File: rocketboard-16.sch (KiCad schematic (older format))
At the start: 128 parts, among them J1 SWD, K1 MX_RGB, K10 MX_RGB, K11 MX_RGB, K12 MX_RGB, K13 MX_RGB, K14 MX_RGB, K15 MX_RGB, K16 MX_RGB, K2 MX_RGB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

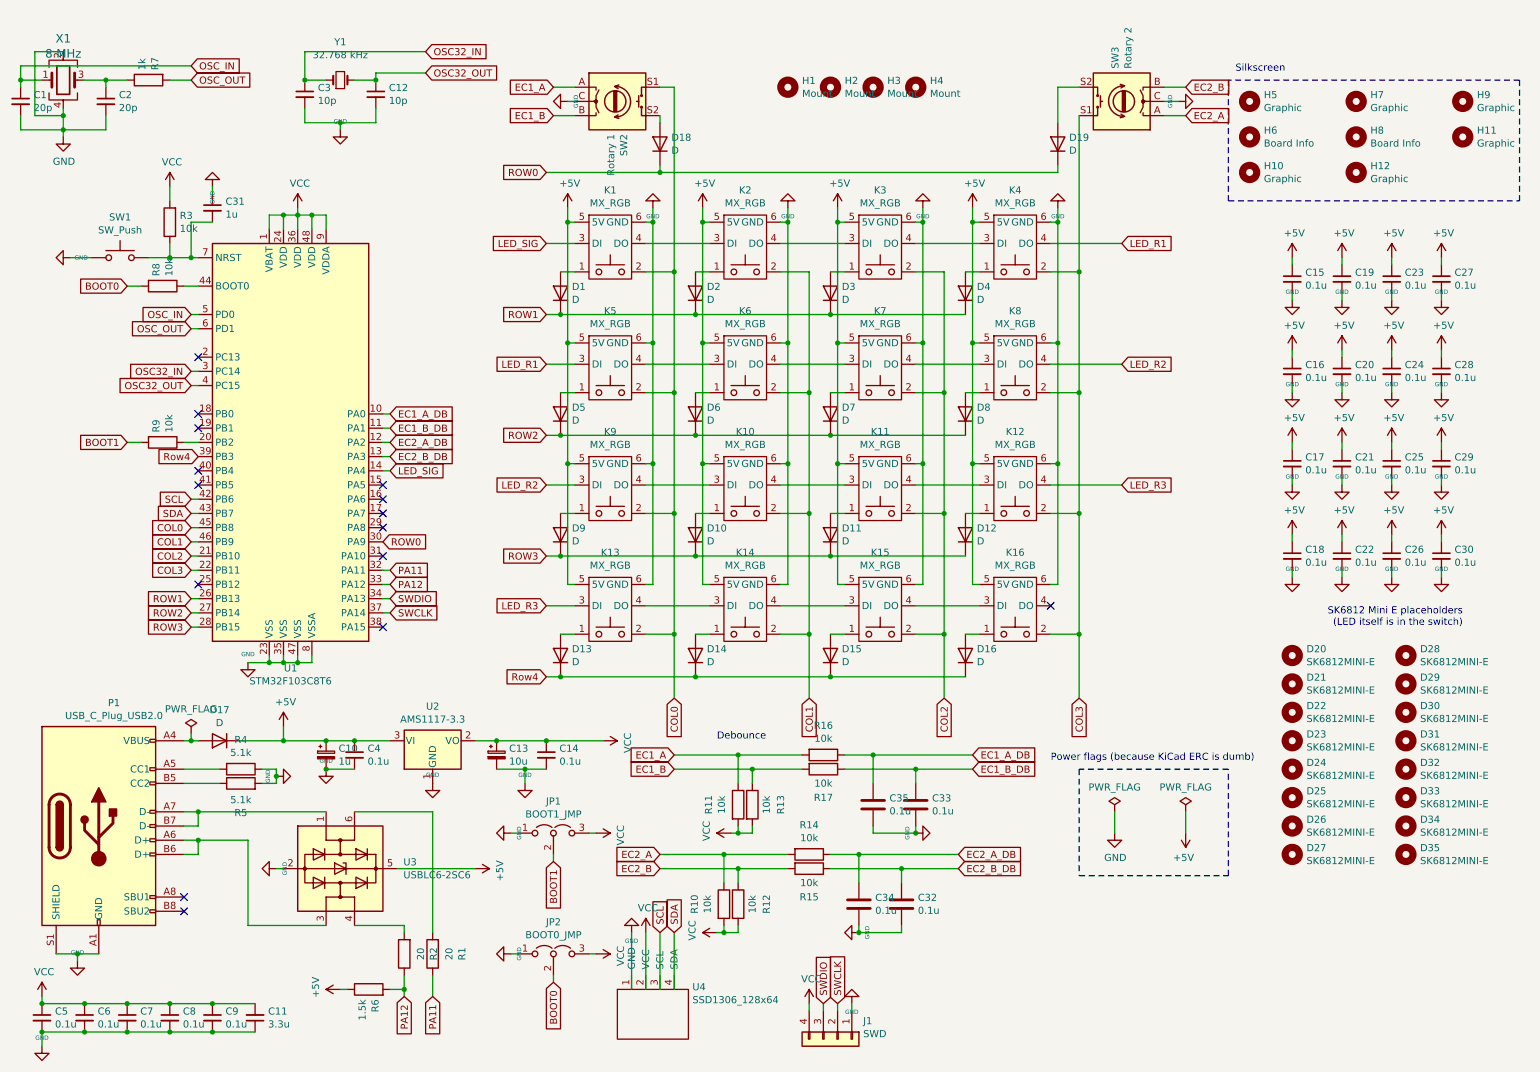
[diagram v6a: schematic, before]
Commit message: Added in a level shifting circuit for the LED signal (needs 5v sig, not 3.3v), added a 10uf cap on the 5v line for smoothing out possible spikey power draw from LEDs, and added test points on +5v, VCC, and GND
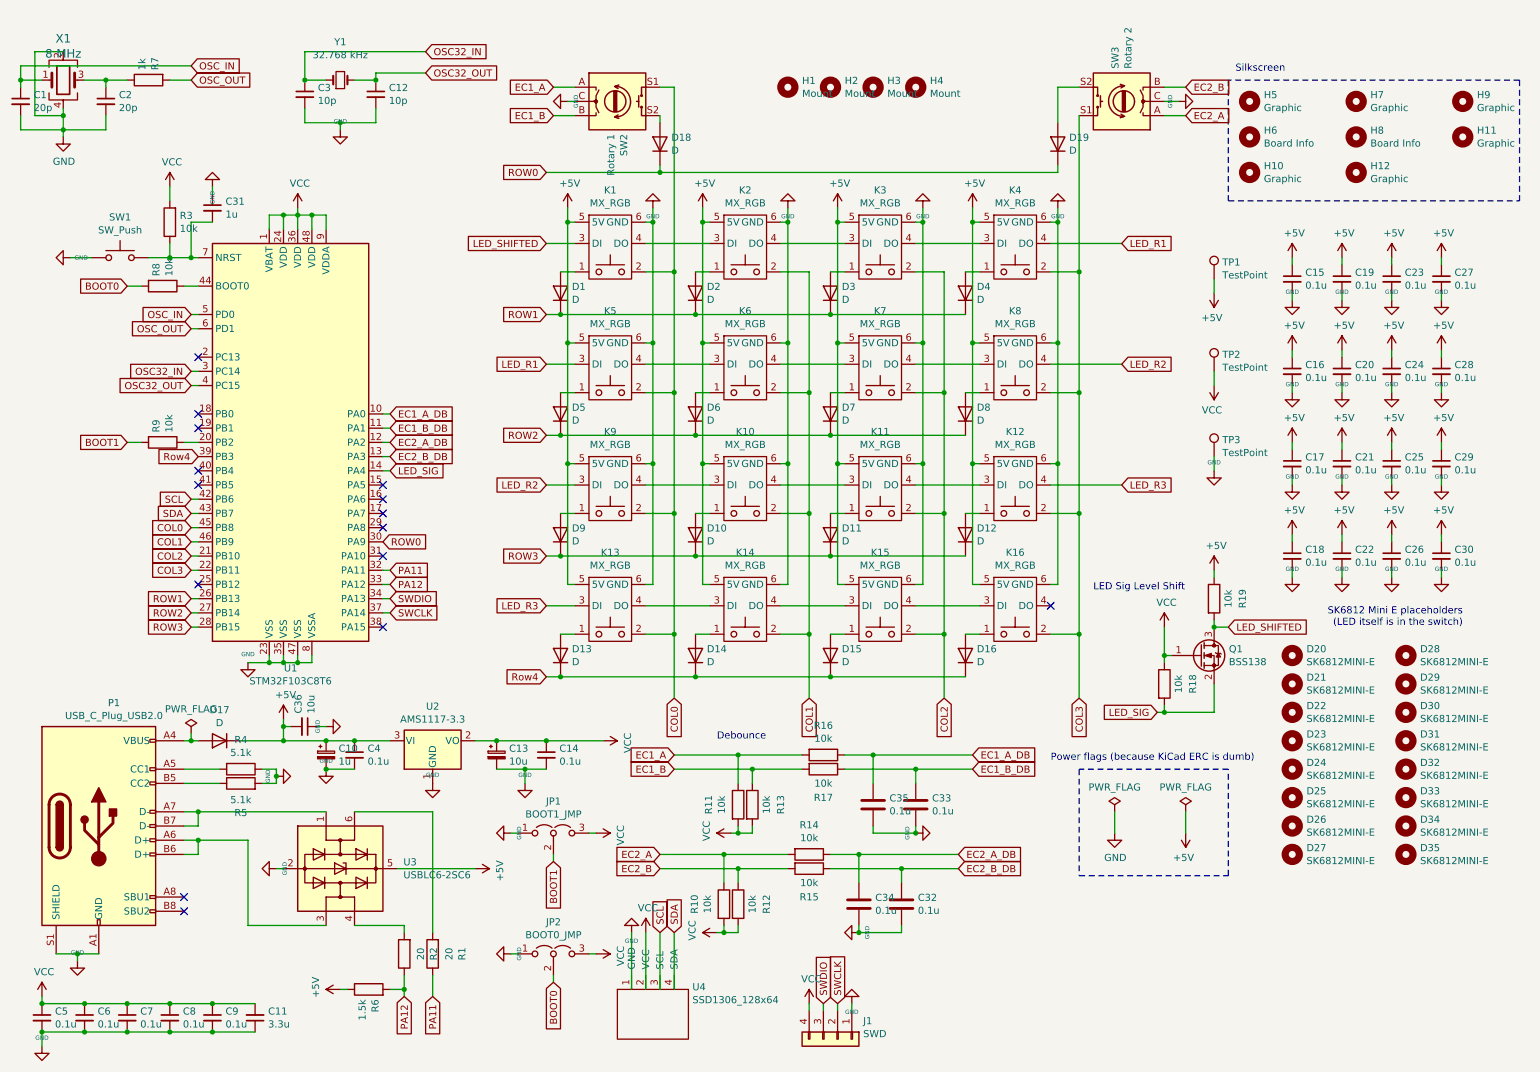
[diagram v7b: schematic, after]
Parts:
- added C36: 10u, Capacitor_SMD:C_0603_1608Metric, symbol Device:C_Small
- added Q1: BSS138, Package_TO_SOT_SMD:SOT-23, symbol Transistor_FET:BSS138
- added R18, R19: 10k, Resistor_SMD:R_0603_1608Metric, symbol Device:R
- added TP1, TP2, TP3: TestPoint, TestPoint:TestPoint_Pad_D1.0mm, symbol Connector:TestPoint
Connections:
- net +5V: now also C36.2, R19.1, TP1.1
- net GND: now also C36.1, TP3.1
- net LED_SIG: now also Q1.2 (S), R18.2; no longer K1.3 (DI)
- net VCC: now also Q1.1 (G), R18.1, TP2.1
- new net LED_SHIFTED: K1.3 (DI), Q1.3 (D), R19.2
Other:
- note added: "LED Sig Level Shift"
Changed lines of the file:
@@
 L power:+5V #PWR010
 U 1 1 5F3A3D06
-P 2450 5400
-F 0 "#PWR010" H 2450 5250 50  0001 C CNN
-F 1 "+5V" H 2465 5573 50  0000 C CNN
-F 2 "" H 2450 5400 50  0001 C CNN
-F 3 "" H 2450 5400 50  0001 C CNN
-	1    2450 5400
+P 2450 5350
+F 0 "#PWR010" H 2450 5200 50  0001 C CNN
+F 1 "+5V" H 2465 5523 50  0000 C CNN
+F 2 "" H 2450 5350 50  0001 C CNN
+F 3 "" H 2450 5350 50  0001 C CNN
+	1    2450 5350
 	1    0    0    -1
 $EndComp
@@
 Text GLabel 3200 3600 2    50   Input ~ 0
 LED_SIG
-Text GLabel 4300 2000 0    50   Input ~ 0
-LED_SIG
 $Comp
 L Device:R R7
@@
 Wire Wire Line
 	4300 5500 4700 5500
-Wire Wire Line
-	2450 5400 2450 5500
 Connection ~ 2450 5500
 Wire Wire Line
@@
 	1    0    0    -1
 $EndComp
+$Comp
+L Device:R R18
+U 1 1 5F971C6A
+P 8650 5100
+F 0 "R18" V 8850 5100 50  0000 C CNN
+F 1 "10k" V 8750 5100 50  0000 C CNN
+F 2 "Resistor_SMD:R_0603_1608Metric" V 8580 5100 50  0001 C CNN
+F 3 "~" H 8650 5100 50  0001 C CNN
+	1    8650 5100
+	1    0    0    -1
+$EndComp
+$Comp
+L Device:R R19
+U 1 1 5F9730D1
+P 9000 4500
+F 0 "R19" V 9200 4500 50  0000 C CNN
+F 1 "10k" V 9100 4500 50  0000 C CNN
+F 2 "Resistor_SMD:R_0603_1608Metric" V 8930 4500 50  0001 C CNN
+F 3 "~" H 9000 4500 50  0001 C CNN
+	1    9000 4500
+	1    0    0    -1
+$EndComp
+$Comp
+L Transistor_FET:BSS138 Q1
+U 1 1 5F9744B4
+P 8900 4900
+F 0 "Q1" H 9104 4946 50  0000 L CNN
+F 1 "BSS138" H 9104 4855 50  0000 L CNN
+F 2 "Package_TO_SOT_SMD:SOT-23" H 9100 4825 50  0001 L CIN
+F 3 "https://www.fairchildsemi.com/datasheets/BS/BSS138.pdf" H 8900 4900 50  0001 L CNN
+	1    8900 4900
+	1    0    0    -1
+$EndComp
+$Comp
+L power:+5V #PWR065
+U 1 1 5F97B5D2
+P 9000 4300
+F 0 "#PWR065" H 9000 4150 50  0001 C CNN
+F 1 "+5V" H 9015 4473 50  0000 C CNN
+F 2 "" H 9000 4300 50  0001 C CNN
+F 3 "" H 9000 4300 50  0001 C CNN
+	1    9000 4300
+	1    0    0    -1
+$EndComp
+$Comp
+L power:VCC #PWR064
+U 1 1 5F9A2AE6
+P 8650 4700
+F 0 "#PWR064" H 8650 4550 50  0001 C CNN
+F 1 "VCC" H 8665 4873 50  0000 C CNN
+F 2 "" H 8650 4700 50  0001 C CNN
+F 3 "" H 8650 4700 50  0001 C CNN
+	1    8650 4700
+	1    0    0    -1
+$EndComp
+Text GLabel 8600 5300 0    50   Input ~ 0
+LED_SIG
+Wire Wire Line
+	8650 4900 8700 4900
+Wire Wire Line
+	9000 4300 9000 4350
+Wire Wire Line
+	9000 4700 9000 4650
+Text GLabel 9100 4700 2    50   Input ~ 0
+LED_SHIFTED
+Wire Wire Line
+	9100 4700 9000 4700
+Connection ~ 9000 4700
+Text Notes 8150 4450 0    50   ~ 0
+LED Sig Level Shift
+Text GLabel 4300 2000 0    50   Input ~ 0
+LED_SHIFTED
+Wire Wire Line
+	8650 4700 8650 4900
+Wire Wire Line
+	8650 4950 8650 4900
+Connection ~ 8650 4900
+Wire Wire Line
+	8600 5300 8650 5300
+Wire Wire Line
+	9000 5300 9000 5100
+Wire Wire Line
+	8650 5250 8650 5300
+Connection ~ 8650 5300
+Wire Wire Line
+	8650 5300 9000 5300
+Wire Wire Line
+	2450 5350 2450 5400
+$Comp
+L Device:C_Small C36
+U 1 1 600E708F
+P 2600 5400
+F 0 "C36" H 2508 5354 50  0000 R CNN
+F 1 "10u" H 2508 5445 50  0000 R CNN
+F 2 "Capacitor_SMD:C_0603_1608Metric" H 2600 5400 50  0001 C CNN
+F 3 "~" H 2600 5400 50  0001 C CNN
+	1    2600 5400
+	0    1    1    0
+$EndComp
+Wire Wire Line
+	2450 5400 2500 5400
+Connection ~ 2450 5400
+Wire Wire Line
+	2450 5400 2450 5500
+$Comp
+L power:GND #PWR066
+U 1 1 60138915
+P 2750 5400
+F 0 "#PWR066" H 2750 5450 20  0001 C CNN
+F 1 "GND" H 2750 5459 30  0000 C CNN
+F 2 "" H 2750 5400 60  0000 C CNN
+F 3 "" H 2750 5400 60  0000 C CNN
+	1    2750 5400
+	0    -1   -1   0
+$EndComp
+Wire Wire Line
+	2700 5400 2750 5400
+$Comp
+L Connector:TestPoint TP1
+U 1 1 6018BF84
+P 9000 2250
+F 0 "TP1" H 9058 2368 50  0000 L CNN
+F 1 "TestPoint" H 9058 2277 50  0000 L CNN
+F 2 "TestPoint:TestPoint_Pad_D1.0mm" H 9200 2250 50  0001 C CNN
+F 3 "~" H 9200 2250 50  0001 C CNN
+	1    9000 2250
+	1    0    0    -1
+$EndComp
+$Comp
+L Connector:TestPoint TP2
+U 1 1 6018D699
+P 9000 2900
+F 0 "TP2" H 9058 3018 50  0000 L CNN
+F 1 "TestPoint" H 9058 2927 50  0000 L CNN
+F 2 "TestPoint:TestPoint_Pad_D1.0mm" H 9200 2900 50  0001 C CNN
+F 3 "~" H 9200 2900 50  0001 C CNN
+	1    9000 2900
+	1    0    0    -1
+$EndComp
+$Comp
+L power:+5V #PWR067
+U 1 1 6018EE42
+P 9000 2350
+F 0 "#PWR067" H 9000 2200 50  0001 C CNN
+F 1 "+5V" H 9015 2523 50  0000 C CNN
+F 2 "" H 9000 2350 50  0001 C CNN
+F 3 "" H 9000 2350 50  0001 C CNN
+	1    9000 2350
+	-1   0    0    1
+$EndComp
+Wire Wire Line
+	9000 2250 9000 2350
+$Comp
+L power:VCC #PWR068
+U 1 1 602376AF
+P 9000 3000
+F 0 "#PWR068" H 9000 2850 50  0001 C CNN
+F 1 "VCC" H 9015 3173 50  0000 C CNN
+F 2 "" H 9000 3000 50  0001 C CNN
+F 3 "" H 9000 3000 50  0001 C CNN
+	1    9000 3000
+	-1   0    0    1
+$EndComp
+Wire Wire Line
+	9000 2900 9000 3000
+$Comp
+L Connector:TestPoint TP3
+U 1 1 602D65EE
+P 9000 3500
+F 0 "TP3" H 9058 3618 50  0000 L CNN
+F 1 "TestPoint" H 9058 3527 50  0000 L CNN
+F 2 "TestPoint:TestPoint_Pad_D1.0mm" H 9200 3500 50  0001 C CNN
+F 3 "~" H 9200 3500 50  0001 C CNN
+	1    9000 3500
+	1    0    0    -1
+$EndComp
+$Comp
+L power:GND #PWR069
+U 1 1 602FF07E
+P 9000 3600
+F 0 "#PWR069" H 9000 3650 20  0001 C CNN
+F 1 "GND" H 9000 3659 30  0000 C CNN
+F 2 "" H 9000 3600 60  0000 C CNN
+F 3 "" H 9000 3600 60  0000 C CNN
+	1    9000 3600
+	1    0    0    -1
+$EndComp
+Wire Wire Line
+	9000 3500 9000 3600
 $EndSCHEMATC

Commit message: Updated design to include 10k resistors between boot select jumpers and MCU
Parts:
- added R20, R21: 10k, Resistor_SMD:R_0603_1608Metric, symbol Device:R
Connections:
- net BOOT0: now also R21.2; no longer JP2.2 (C)
- net BOOT1: now also R20.2; no longer JP1.2 (C)
- new net: JP1.2 (C), R20.1
- new net: JP2.2 (C), R21.1
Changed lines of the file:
@@
 Text GLabel 1350 3400 0    50   Input ~ 0
 BOOT1
-Text GLabel 4350 7200 3    50   Input ~ 0
+Text GLabel 4350 7600 2    50   Input ~ 0
 BOOT0
-Text GLabel 4350 6350 3    50   Input ~ 0
+Text GLabel 4350 6700 2    50   Input ~ 0
 BOOT1
 $Comp
@@
 Wire Wire Line
 	9000 3500 9000 3600
+$Comp
+L Device:R R21
+U 1 1 60382A16
+P 4350 7350
+F 0 "R21" V 4143 7350 50  0000 C CNN
+F 1 "10k" V 4234 7350 50  0000 C CNN
+F 2 "Resistor_SMD:R_0603_1608Metric" V 4280 7350 50  0001 C CNN
+F 3 "~" H 4350 7350 50  0001 C CNN
+	1    4350 7350
+	1    0    0    -1
+$EndComp
+Wire Wire Line
+	4350 7600 4350 7500
+$Comp
+L Device:R R20
+U 1 1 603FDBF5
+P 4350 6500
+F 0 "R20" V 4143 6500 50  0000 C CNN
+F 1 "10k" V 4234 6500 50  0000 C CNN
+F 2 "Resistor_SMD:R_0603_1608Metric" V 4280 6500 50  0001 C CNN
+F 3 "~" H 4350 6500 50  0001 C CNN
+	1    4350 6500
+	1    0    0    -1
+$EndComp
+Wire Wire Line
+	4350 6650 4350 6700
 $EndSCHEMATC
